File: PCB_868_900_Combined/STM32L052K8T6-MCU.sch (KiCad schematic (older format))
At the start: 26 parts, among them J2 20021121-00010C4LF, J5 0475890001-MicroUSBPort, P1 61301621121, SW2 B3U-1000P, U3 STM32L052C8T6, X3 ABM10-166-12.000MHZ-T3

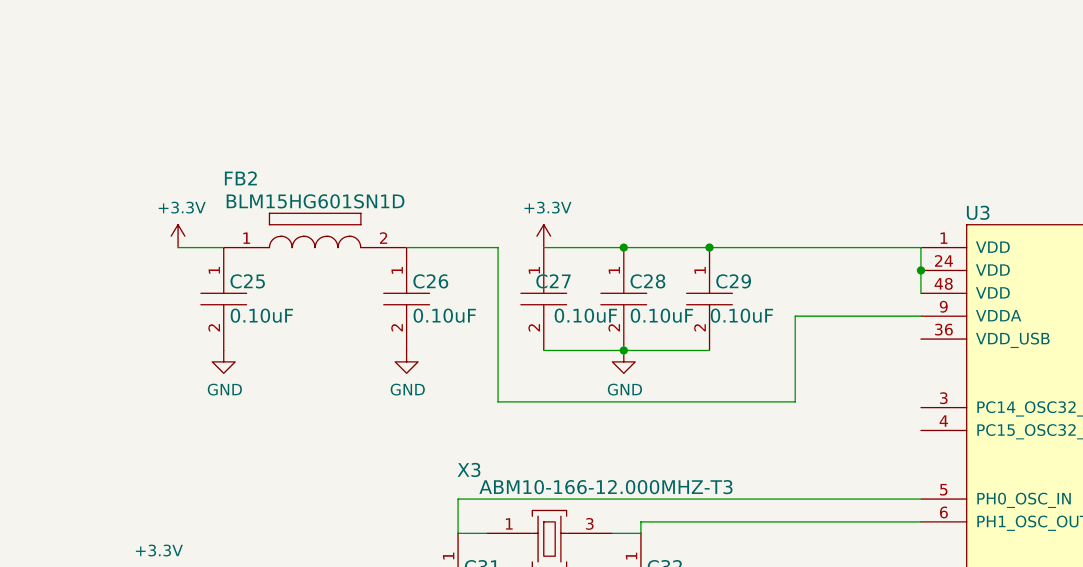
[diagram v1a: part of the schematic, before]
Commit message: USB VDD
Found schematic bug, USB VDD was not tied to 3V3 supply or applied a
bypass cap, this has been resolved in both implementations of the S1G.
STM32L0 program manual added to the datasheets collection for the
project. Schematic PDFs updated.
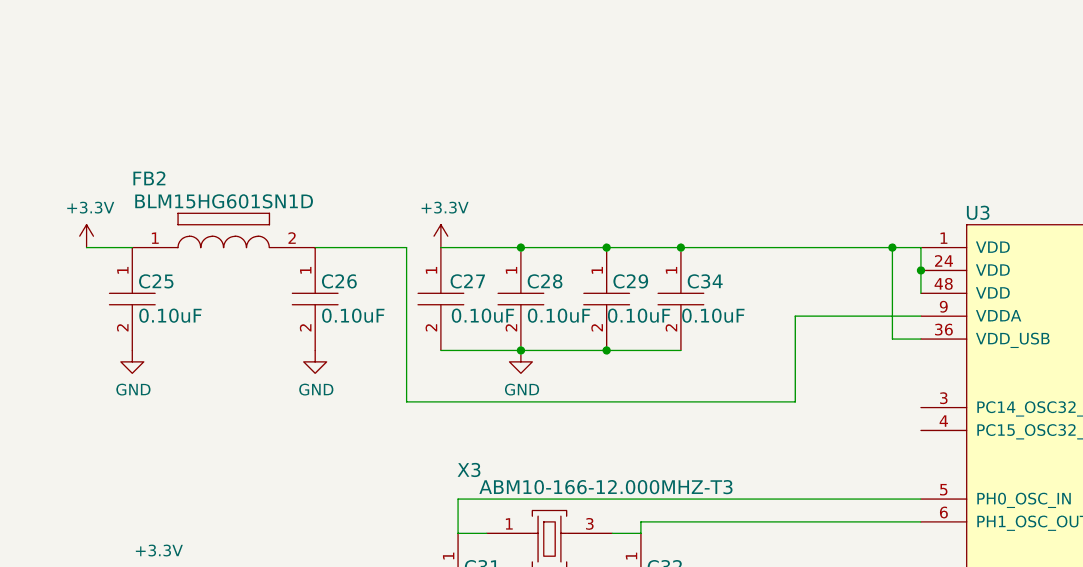
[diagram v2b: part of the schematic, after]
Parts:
- added C34: CL05B104JP5NNNC, PCB_Footprints:C0402, symbol CL05B104JP5NNNC
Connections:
- wire segments 92 -> 94
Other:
- moved on the sheet: C25, C26, C27, C28, C29, FB2

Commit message: Radio Reference Schematic Errors
Some errors transcribing ADI's reference shcematic. 0.22uF caps added to
pins that needed it etc.
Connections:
- net labels added: HB_1, HB_2
- wire segments 94 -> 95
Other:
- moved on the sheet: DA1, LED2, LED3, R7, R8, R9
